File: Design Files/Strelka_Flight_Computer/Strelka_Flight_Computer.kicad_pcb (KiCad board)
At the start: 2 copper layers, 99 parts, among them J1 2-3S_LiPo_LARGE_HOLE_XT-30, J2 Conn_01x04, J5 USB_B_Micro, J6 USB_B_Micro, Q1 ??, Q10 AP2300, Q11 AP2300, Q12 AO3401A, Q2 ??, Q3 AO3401A, Q4 AP2300, Q5 AO3401A, Q6 AP2300, Q7 AO3401A, Q8 AP2300, Q9 MMBT2222, SW1 SW_Push, SW2 SW_Push, U1 FP6276BXR-G1, U10 BMX055, U13 LM334M, U14 LM334M, U15 LM334M, U16 LM321, U17 LM321, U18 LM321, U2 AP9101CK6, U3 AMS1117-3.3, U4 RFM95W-915S2, U5 STM32F405RGTx, U6 LM358, U7 USBLC6-2SC6, U8 USBLC6-2SC6, U9 CP2102N-Axx-xQFN28, Y1 Q13FC1350000200, Y2 X322524MOB4SI

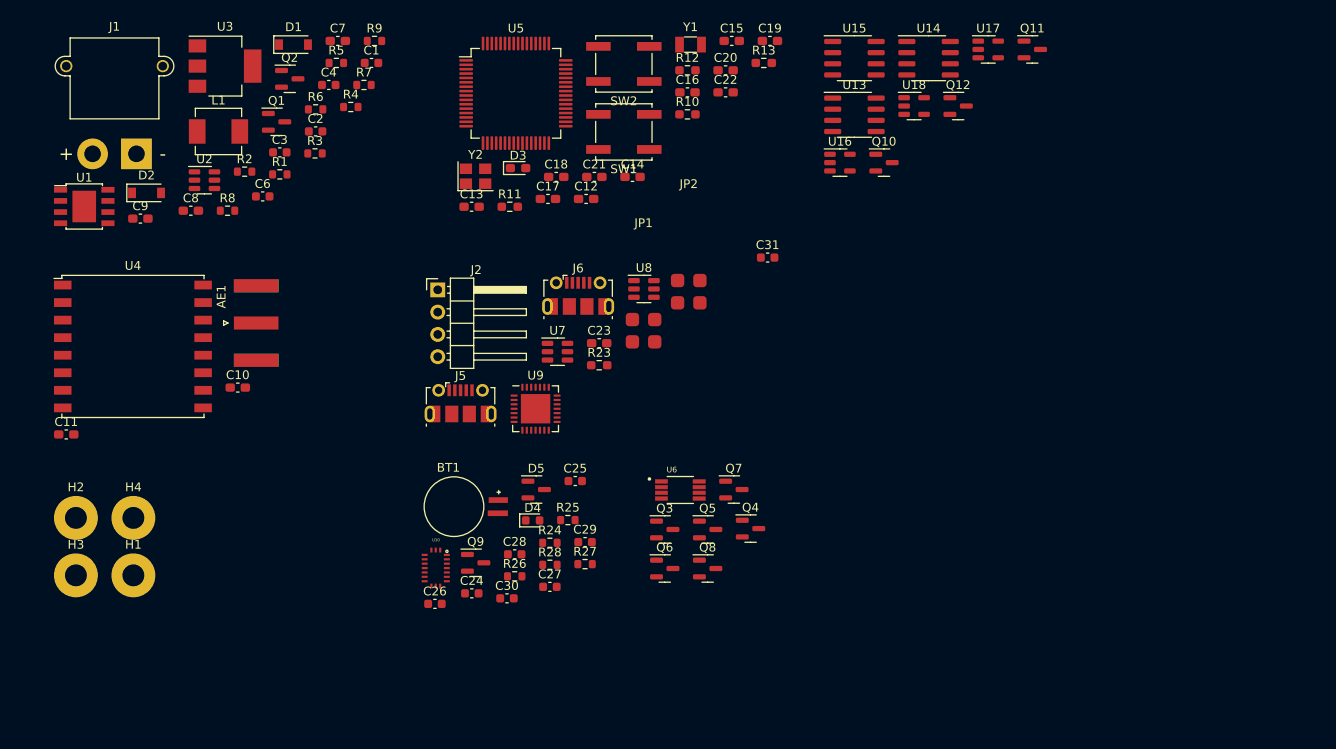
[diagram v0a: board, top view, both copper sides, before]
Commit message: Started writing libraries for board functions
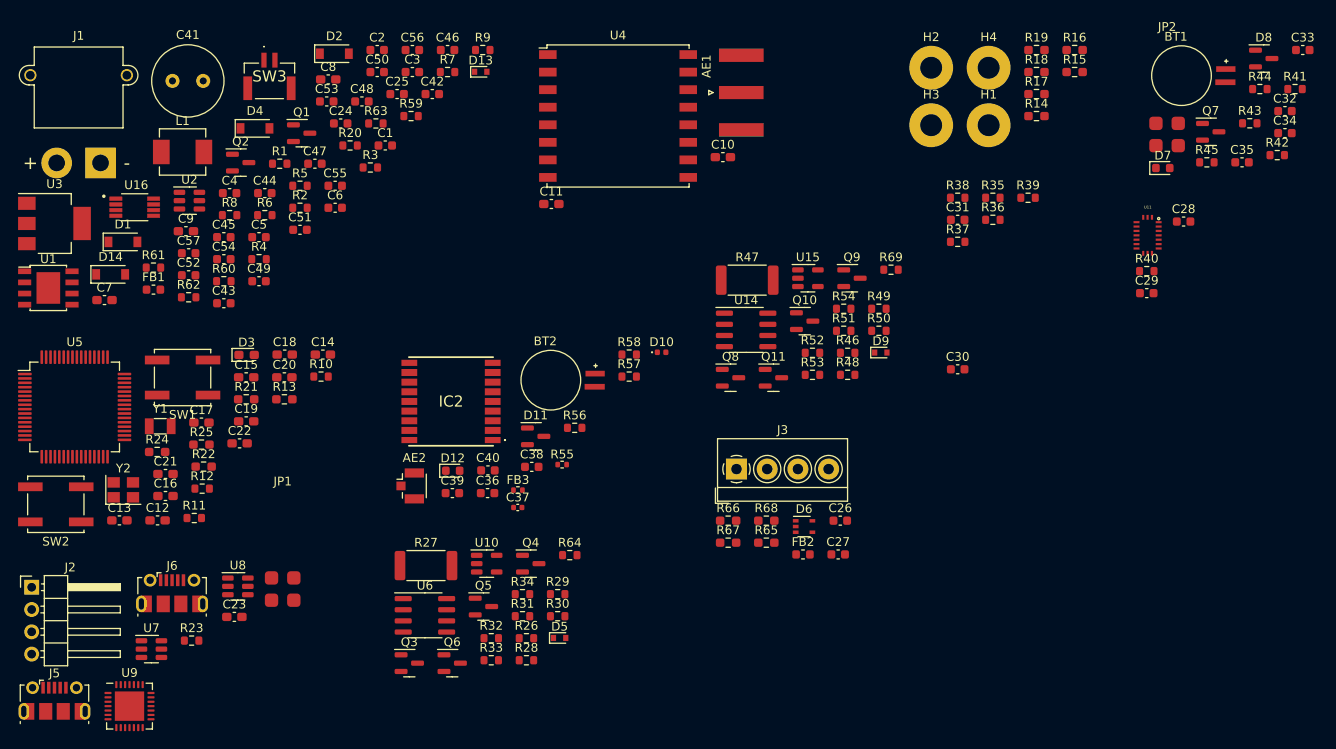
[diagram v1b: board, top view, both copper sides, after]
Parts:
- removed Q12: AO3401A, Package_TO_SOT_SMD:SOT-23
- removed U13: LM334M, Package_SO:SOIC-8_3.9x4.9mm_P1.27mm
- removed U17, U18: LM321, Package_TO_SOT_SMD:SOT-23-5
- added AE2: Antenna_Shield, Connector_Coaxial:U.FL_Hirose_U.FL-R-SMT-1_Vertical, F.Cu at (126.3, 98.8)
- added BT2: MS621FE-FL11E, Footprints:BAT_MS621FE-FL11E, F.Cu at (142.3, 86.8)
- added C32: 100nF, Capacitor_SMD:C_0603_1608Metric, F.Cu at (226.0, 56.1)
- added C33: 10uF, Capacitor_SMD:C_0603_1608Metric, F.Cu at (228.0, 49.1)
- added C34: 100n, Capacitor_SMD:C_0603_1608Metric, F.Cu at (226.0, 58.6)
- added C35: 4.7u, Capacitor_SMD:C_0603_1608Metric, F.Cu at (221.1, 62.0)
- added C36: 100n, Capacitor_SMD:C_0603_1608Metric, F.Cu at (135.1, 99.7)
- added C37: NC, Capacitor_SMD:C_0402_1005Metric, F.Cu at (138.5, 101.3)
- added C38: 4.7u, Capacitor_SMD:C_0603_1608Metric, F.Cu at (140.1, 96.7)
- added C39: 100nF, Capacitor_SMD:C_0603_1608Metric, F.Cu at (131.1, 99.7)
- added C40: 10uF, Capacitor_SMD:C_0603_1608Metric, F.Cu at (135.1, 97.1)
- added C41: 1500u, Capacitor_THT:C_Radial_D8.0mm_H11.5mm_P3.50mm, F.Cu at (99.2, 52.7)
- added C42: NC, Capacitor_SMD:C_0603_1608Metric, F.Cu at (128.8, 54.2)
- added C43: NC, Capacitor_SMD:C_0603_1608Metric, F.Cu at (105.0, 78.0)
- added C44: 2.2u, Capacitor_SMD:C_0603_1608Metric, F.Cu at (109.7, 65.5)
- added C45: 2.2u, Capacitor_SMD:C_0603_1608Metric, F.Cu at (105.0, 70.5)
- added C46: 22u, Capacitor_SMD:C_0603_1608Metric, F.Cu at (130.5, 49.1)
- added C47: 1u, Capacitor_SMD:C_0603_1608Metric, F.Cu at (115.4, 62.1)
- added C48: 0.1u, Capacitor_SMD:C_0603_1608Metric, F.Cu at (120.8, 55.0)
- added C49: NC, Capacitor_SMD:C_0603_1608Metric, F.Cu at (109.0, 75.5)
- added C5: 22u, Capacitor_SMD:C_0603_1608Metric, F.Cu at (109.0, 70.5)
- added C50: NC, Capacitor_SMD:C_0603_1608Metric, F.Cu at (122.5, 51.7)
- added C51: 820p, Capacitor_SMD:C_0603_1608Metric, F.Cu at (113.7, 69.6)
- added C52: NC, Capacitor_SMD:C_0603_1608Metric, F.Cu at (101.0, 74.8)
- added C53: NC, Capacitor_SMD:C_0603_1608Metric, F.Cu at (116.8, 55.0)
- added C54: NC, Capacitor_SMD:C_0603_1608Metric, F.Cu at (105.0, 73.0)
- added C55: 68u, Capacitor_SMD:C_0603_1608Metric, F.Cu at (117.7, 64.6)
- added C56: NC, Capacitor_SMD:C_0603_1608Metric, F.Cu at (126.5, 49.1)
- added C57: NC, Capacitor_SMD:C_0603_1608Metric, F.Cu at (101.0, 72.3)
- added D10: ESD9B3.3ST5G, Diode_SMD:D_0402_1005Metric, F.Cu at (154.9, 83.6)
- added D11: BAT54C, Package_TO_SOT_SMD:SOT-23, F.Cu at (140.6, 93.2)
- added D12: LED_BLUE, LED_SMD:LED_0603_1608Metric, F.Cu at (131.1, 97.1)
- added D13: BZT52C3V6T, Diode_SMD:D_SOD-523, F.Cu at (134.3, 51.6)
- added D14: DSK34, Diode_SMD:D_SOD-123, F.Cu at (92.1, 74.7)
- added D6: SP0504BAJT, Package_TO_SOT_SMD:SOT-353_SC-70-5, F.Cu at (171.2, 103.5)
- added D7: LED_BLUE, LED_SMD:LED_0603_1608Metric, F.Cu at (212.0, 62.6)
- added D8: BAT54C, Package_TO_SOT_SMD:SOT-23, F.Cu at (223.5, 50.1)
- added D9: 1SS388, Diode_SMD:D_SOD-523, F.Cu at (179.9, 83.6)
- added FB1: FerriteBead_Small, Inductor_SMD:L_0603_1608Metric, F.Cu at (97.0, 76.5)
- added FB2: FerriteBead_Small, Inductor_SMD:L_0603_1608Metric, F.Cu at (171.0, 106.6)
- added FB3: HZ1005K182TFB03, Resistor_SMD:R_0402_1005Metric, F.Cu at (138.5, 99.3)
- added IC2: MAX-M10S-00B, Footprints:MAXM10S00B, F.Cu at (130.9, 89.2)
- added J3: DB125-3.5-4P-GN-S, TerminalBlock_4Ucon:TerminalBlock_4Ucon_1x04_P3.50mm_Horizontal, F.Cu at (163.5, 96.9)
- added R14: 0, Resistor_SMD:R_0603_1608Metric_Pad0.98x0.95mm_HandSolder, F.Cu at (197.6, 56.7)
- added R15: 0, Resistor_SMD:R_0603_1608Metric_Pad0.98x0.95mm_HandSolder, F.Cu at (202.0, 51.7)
- added R16: 0, Resistor_SMD:R_0603_1608Metric_Pad0.98x0.95mm_HandSolder, F.Cu at (202.0, 49.1)
- added R17: 0, Resistor_SMD:R_0603_1608Metric_Pad0.98x0.95mm_HandSolder, F.Cu at (197.6, 54.2)
- added R18: 0, Resistor_SMD:R_0603_1608Metric_Pad0.98x0.95mm_HandSolder, F.Cu at (197.6, 51.7)
- added R19: 0, Resistor_SMD:R_0603_1608Metric_Pad0.98x0.95mm_HandSolder, F.Cu at (197.6, 49.1)
- added R20: 0, Resistor_SMD:R_0603_1608Metric, F.Cu at (119.4, 60.0)
- added R21: 10k, Resistor_SMD:R_0603_1608Metric_Pad0.98x0.95mm_HandSolder, F.Cu at (107.6, 89.0)
- added R22: 10k, Resistor_SMD:R_0603_1608Metric_Pad0.98x0.95mm_HandSolder, F.Cu at (102.7, 96.6)
- added R29: 100k, Resistor_SMD:R_0603_1608Metric, F.Cu at (143.1, 111.2)
- added R30: 100k, Resistor_SMD:R_0603_1608Metric, F.Cu at (143.1, 113.7)
- added R31: 1k, Resistor_SMD:R_0603_1608Metric, F.Cu at (139.1, 113.7)
- added R32: 100k, Resistor_SMD:R_0603_1608Metric, F.Cu at (135.5, 116.2)
- added R33: 1k, Resistor_SMD:R_0603_1608Metric, F.Cu at (135.5, 118.7)
- added R34: 1k, Resistor_SMD:R_0603_1608Metric, F.Cu at (139.1, 111.2)
- added R35: 47k, Resistor_SMD:R_0603_1608Metric, F.Cu at (192.7, 66.0)
- added R36: 47k, Resistor_SMD:R_0603_1608Metric, F.Cu at (192.7, 68.5)
- added R37: 47k, Resistor_SMD:R_0603_1608Metric, F.Cu at (188.7, 71.0)
- added R38: 47k, Resistor_SMD:R_0603_1608Metric, F.Cu at (188.7, 66.0)
- added R39: 47k, Resistor_SMD:R_0603_1608Metric, F.Cu at (196.7, 66.0)
- added R40: 0R, Resistor_SMD:R_0603_1608Metric, F.Cu at (210.2, 74.3)
- added R41: 1k, Resistor_SMD:R_0603_1608Metric, F.Cu at (227.1, 53.6)
- added R42: R_Small, Resistor_SMD:R_0603_1608Metric, F.Cu at (225.1, 61.1)
- added R43: 1k, Resistor_SMD:R_0603_1608Metric, F.Cu at (222.0, 57.5)
- added R44: 1k, Resistor_SMD:R_0603_1608Metric, F.Cu at (223.1, 53.6)
- added R45: 1k, Resistor_SMD:R_0603_1608Metric, F.Cu at (217.1, 62.0)
- added R46: 64.9R, Resistor_SMD:R_0603_1608Metric, F.Cu at (176.1, 83.7)
- added R47: 2R, Resistor_SMD:R_2512_6332Metric, F.Cu at (164.7, 75.4)
- added R48: 1k, Resistor_SMD:R_0603_1608Metric, F.Cu at (176.1, 86.2)
- added R49: 100k, Resistor_SMD:R_0603_1608Metric, F.Cu at (179.7, 78.6)
- added R50: 100k, Resistor_SMD:R_0603_1608Metric, F.Cu at (179.7, 81.2)
- added R51: 1k, Resistor_SMD:R_0603_1608Metric, F.Cu at (175.7, 81.2)
- added R52: 100k, Resistor_SMD:R_0603_1608Metric, F.Cu at (172.1, 83.7)
- added R53: 1k, Resistor_SMD:R_0603_1608Metric, F.Cu at (172.1, 86.2)
- added R54: 1k, Resistor_SMD:R_0603_1608Metric, F.Cu at (175.7, 78.6)
- added R55: 0R, Resistor_SMD:R_0402_1005Metric, F.Cu at (143.6, 96.4)
- added R56: 1k, Resistor_SMD:R_0603_1608Metric, F.Cu at (145.0, 92.2)
- added R57: 1k, Resistor_SMD:R_0603_1608Metric, F.Cu at (151.2, 86.4)
- added R58: 0R, Resistor_SMD:R_0603_1608Metric, F.Cu at (151.2, 83.9)
- added R59: 13k, Resistor_SMD:R_0603_1608Metric, F.Cu at (126.4, 56.7)
- added R60: 47k, Resistor_SMD:R_0603_1608Metric, F.Cu at (105.0, 75.5)
- added R61: 56.2k, Resistor_SMD:R_0603_1608Metric, F.Cu at (97.0, 74.0)
- added R62: 82k, Resistor_SMD:R_0603_1608Metric, F.Cu at (101.0, 77.3)
- added R63: 27k, Resistor_SMD:R_0603_1608Metric, F.Cu at (122.4, 57.5)
- added R64: 100k, Resistor_SMD:R_0603_1608Metric, F.Cu at (144.5, 106.7)
- added R65: 33, Resistor_SMD:R_0603_1608Metric_Pad0.98x0.95mm_HandSolder, F.Cu at (166.9, 105.3)
- added R66: 33, Resistor_SMD:R_0603_1608Metric_Pad0.98x0.95mm_HandSolder, F.Cu at (162.5, 102.8)
- added R67: 33, Resistor_SMD:R_0603_1608Metric_Pad0.98x0.95mm_HandSolder, F.Cu at (162.5, 105.3)
- added R68: 33, Resistor_SMD:R_0603_1608Metric_Pad0.98x0.95mm_HandSolder, F.Cu at (166.9, 102.8)
- added R69: 100k, Resistor_SMD:R_0603_1608Metric, F.Cu at (181.1, 74.2)
- added SW3: SW_DIP_x01, Footprints:SM02BGHSTBLFSN, F.Cu at (110.2, 52.1)
- added U11: BMX055, Footprints:BMX055, F.Cu at (210.3, 70.3)
- C24, C25: value 100nF -> NC
- C26, C27: value 100nF -> 2.2u
- C28: value 10uF -> 100nF
- C29: value 100n -> 100nF
- C30: value 4.7u -> 100nF
- C4: value 22u -> NC
- D4: value LED_BLUE -> B5819W; footprint LED_SMD:LED_0603_1608Metric -> Diode_SMD:D_SOD-123
- D5: value BAT54C -> 1SS388; footprint Package_TO_SOT_SMD:SOT-23 -> Diode_SMD:D_SOD-523
- J1: value 2-3S_LiPo_LARGE_HOLE_XT-30 -> 1S_LiPo_LARGE_HOLE_XT-30
- Q11, Q6: value AP2300 -> MMBT2222
- Q4, Q8: value AP2300 -> AO3401A
- Q5: value AO3401A -> AP2300
- Q7: value AO3401A -> MMBT2222
- Q9: value MMBT2222 -> AO3401A
- R10, R11, R12, R23: footprint Resistor_SMD:R_0603_1608Metric_Pad0.98x0.95mm_HandSolder -> Resistor_SMD:R_0603_1608Metric
- R24: value 1k -> NC; footprint Resistor_SMD:R_0603_1608Metric -> Resistor_SMD:R_0603_1608Metric_Pad0.98x0.95mm_HandSolder
- R25: value R_Small -> 10k; footprint Resistor_SMD:R_0603_1608Metric -> Resistor_SMD:R_0603_1608Metric_Pad0.98x0.95mm_HandSolder
- R26: value 1k -> 64.9R
- R27: value 1k -> 2R; footprint Resistor_SMD:R_0603_1608Metric -> Resistor_SMD:R_2512_6332Metric
- U10: value BMX055 -> LM321; footprint Footprints:BMX055 -> Package_TO_SOT_SMD:SOT-23-5
- U15: value LM334M -> LM321; footprint Package_SO:SOIC-8_3.9x4.9mm_P1.27mm -> Package_TO_SOT_SMD:SOT-23-5
- U16: value LM321 -> TPS61085DGKR; footprint Package_TO_SOT_SMD:SOT-23-5 -> Footprints:SOP65P490X110-8N
- U6: value LM358 -> LM334M; footprint Footprints:SOP65P490X110-8N -> Package_SO:SOIC-8_3.9x4.9mm_P1.27mm
- moved H1 110.2 mm to (192.2, 57.7)
- moved H2 110.2 mm to (185.6, 51.2)
- moved H3 110.2 mm to (185.6, 57.7)
- moved H4 110.2 mm to (192.2, 51.2)
- moved BT1 96.4 mm to (214.2, 52.1)
- moved C28 85.1 mm to (214.4, 68.7)
- moved SW2 81.9 mm to (85.9, 100.9)
- moved U16 80.5 mm to (94.9, 67.1)
- moved C16 75.2 mm to (98.4, 100.0)
- moved Y1 74.5 mm to (97.8, 92.0)
- moved C19 73.8 mm to (107.6, 91.5)
- moved R12 73.0 mm to (102.6, 99.1)
- moved C29 70.0 mm to (210.2, 76.9)
- moved C22 68.3 mm to (106.8, 94.0)
- moved Q7 67.9 mm to (217.5, 58.5)
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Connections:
- net /Continuity_Testing/AUX+ renamed Net-(D9-Pad2)
- net /Data_Interfaces/RX_RADIO renamed /Data_Interfaces/TX_CP2102
- net /Data_Interfaces/TX_RADIO renamed /Data_Interfaces/RX_CP2102
- net /Power/BUCK_EN renamed /Power/BOOST_EN
- net Net-(Q7-Pad2) renamed /Sensors/L80-M39/GPS_RESET
- BT1 pad +: /Sensors/V_BKCP -> /Sensors/L80-M39/V_BKCP
- C24 pad 1: VDD -> VDC
- C25 pad 1: VDD -> VDC
- C26 pad 1: VDD -> GND
- C26 pad 2: GND -> +5VD
- C27 pad 1: VDD -> GND
- C27 pad 2: GND -> Net-(C27-Pad2)
- C28 pad 1: VDD -> +3V3
- C29 pad 1: /Sensors/V_BKCP -> +3V3
- C30 pad 1: /Sensors/V_BKCP -> +3V3
- C31 pad 1: VDD -> +3V3
- C4 pad 1: GND -> VDC
- C4 pad 2: +5VA -> GND
- D1 pad 1: VDC -> Net-(D1-Pad1)
- D4 pad 1: GND -> VBUS
- D4 pad 2: Net-(D4-Pad2) -> +5VD
- D5 pad 1: VDD -> /Actuators/Ematch_Drogue1/EMATCH+
- D5 pad 2: unconnected-(D5-Pad2) -> Net-(D5-Pad2)
- JP2 pad 1: Net-(JP2-Pad1) -> /Sensors/RXD2_GPS
- JP2 pad 2: /Data_Interfaces/RTS_RADIO -> Net-(JP2-Pad2)
- JP2 pad 3: Net-(JP2-Pad3) -> /Sensors/TXD2_GPS
- JP2 pad 4: /Data_Interfaces/CTS_RADIO -> Net-(JP2-Pad4)
- Q1 pad 2: VDC -> Net-(D1-Pad1)
- Q10 pad 3: /Continuity_Testing/DROGUE- -> /Actuators/Ematch_Main/EMATCH-
- Q11 pad 2: GND -> Net-(Q11-Pad2)
- Q11 pad 3: /Continuity_Testing/AUX- -> GND
- Q2 pad 3: +5VA -> Net-(Q2-Pad3)
- Q3 pad 2: Net-(Q3-Pad2) -> +3V3
- Q3 pad 3: /Actuators/MAIN+ -> Net-(Q3-Pad3)
- Q4 pad 2: GND -> Net-(Q4-Pad2)
- Q4 pad 3: /Actuators/MAIN- -> /Actuators/Ematch_Drogue1/EMATCH+
- Q5 pad 2: Net-(Q5-Pad2) -> GND
- Q5 pad 3: /Actuators/DROGUE+ -> /Actuators/Ematch_Drogue1/EMATCH-
- Q6 pad 2: GND -> Net-(Q4-Pad1)
- Q6 pad 3: /Actuators/DROGUE- -> GND
- Q7 pad 3: /Actuators/AUX+ -> GND
- Q8 pad 2: GND -> +3V3
- Q8 pad 3: /Actuators/AUX- -> Net-(Q8-Pad3)
- Q9 pad 1: Net-(Q9-Pad1) -> Net-(Q11-Pad2)
- Q9 pad 2: /Sensors/GPS_RESET -> Net-(Q9-Pad2)
- Q9 pad 3: GND -> /Actuators/Ematch_Main/EMATCH+
- R10 pad 1: GND -> Net-(R10-Pad1)
- R10 pad 2: Net-(R10-Pad2) -> GND
- R23 pad 1: Net-(R23-Pad1) -> +3V3
- R23 pad 2: +3V3 -> Net-(R23-Pad2)
- R24 pad 1: Net-(R24-Pad1) -> /STM32F405/SD_DET
- R24 pad 2: Net-(D4-Pad2) -> +3V3
- R25 pad 1: Net-(R24-Pad1) -> GND
- R25 pad 2: /Sensors/GPS_PPS -> /STM32F405/SD_DET
- R26 pad 1: /Sensors/GPS_RST -> Net-(D5-Pad2)
- R26 pad 2: Net-(Q9-Pad1) -> Net-(R26-Pad2)
- R27 pad 1: Net-(Q9-Pad1) -> VDC
- R27 pad 2: GND -> Net-(Q4-Pad2)
- R28 pad 1: /Sensors/V_BKCP -> Net-(Q3-Pad1)
- R28 pad 2: Net-(D5-Pad3) -> /Actuators/CONT_TEST_EN
- R5 pad 2: +5VA -> Net-(C44-Pad2)
- SW1 pad 2: Net-(R10-Pad2) -> Net-(R10-Pad1)
- U1 pad 8: +5VA -> Net-(C44-Pad2)
- U10 pad 1: /Sensors/BMX_Int_2 -> /Actuators/Ematch_Drogue1/EMATCH+
- U10 pad 2: /Sensors/BMX_DRDYM -> +3V3
- U10 pad 3: VDD -> Net-(R32-Pad2)
- U10 pad 4: GND -> /Actuators/DROGUE_CONT
- U10 pad 5: unconnected-(U10-Pad5) -> GND
- U14 pad 4: VDC -> Net-(Q8-Pad3)
- U15 pad 1: unconnected-(U15-Pad1) -> /Actuators/Ematch_Main/EMATCH+
- U15 pad 2: /Continuity_Testing/MAIN+ -> +3V3
- U15 pad 3: /Continuity_Testing/MAIN+ -> Net-(R52-Pad2)
- U15 pad 4: Net-(Q12-Pad3) -> /Actuators/MAIN_CONT
- U15 pad 5: (no net) -> GND
- U16 pad 2: +3V3 -> Net-(R62-Pad1)
- U16 pad 3: Net-(R30-Pad2) -> VDC
- U16 pad 4: /Continuity_Testing/DROGUE_Cont -> GND
- U16 pad 5: GND -> Net-(D14-Pad2)
- U5 pad 1: unconnected-(U5-Pad1) -> +3V3
- U5 pad 10: unconnected-(U5-Pad10) -> /STM32F405/SPI2_MISO
- U5 pad 11: unconnected-(U5-Pad11) -> /STM32F405/SPI2_MOSI
- U5 pad 14: /Data_Interfaces/CTS_2 -> /Actuators/MAIN_L
- U5 pad 15: /Data_Interfaces/RTS_2 -> /Actuators/MAIN_H
- U5 pad 16: /Data_Interfaces/TX_2 -> /Actuators/DROGUE_CONT
- U5 pad 17: /Data_Interfaces/RX_2 -> /Actuators/MAIN_CONT
- U5 pad 2: unconnected-(U5-Pad2) -> /Actuators/CONT_TEST_EN
- U5 pad 24: unconnected-(U5-Pad24) -> /STM32F405/INT_IN1
- U5 pad 25: unconnected-(U5-Pad25) -> /STM32F405/INT_IN2
- U5 pad 26: /915MHz_Radio/RESET_RF -> unconnected-(U5-Pad26)
- U5 pad 27: /915MHz_Radio/IO0_RF -> unconnected-(U5-Pad27)
- U5 pad 29: /915MHz_Radio/IO1_RF -> /STM32F405/I2C2_SCL
- U5 pad 30: /915MHz_Radio/IO2_RF -> /STM32F405/I2C2_SDA
- U5 pad 33: /915MHz_Radio/IO3_RF -> /STM32F405/SPI2_NSS4
- U5 pad 34: /915MHz_Radio/IO4_RF -> /STM32F405/SPI2_SCK
- U5 pad 37: unconnected-(U5-Pad37) -> /STM32F405/INT_IN3
- U5 pad 38: unconnected-(U5-Pad38) -> /STM32F405/SD_DET
- U5 pad 39: unconnected-(U5-Pad39) -> /STM32F405/SDIO_D0
- U5 pad 40: unconnected-(U5-Pad40) -> /STM32F405/SDIO_D1
- U5 pad 41: /915MHz_Radio/IO5_RF -> /Actuators/DROGUE_H
- U5 pad 44: /Data_Interfaces/CTS_RADIO -> /915MHz_Radio/IO0_RF
- U5 pad 45: /Data_Interfaces/RTS_RADIO -> /STM32F405/SPI2_NSS3
- U5 pad 50: unconnected-(U5-Pad50) -> /Actuators/EXT_SPI_CS
- U5 pad 51: unconnected-(U5-Pad51) -> /STM32F405/SDIO_D2
- U5 pad 52: unconnected-(U5-Pad52) -> /STM32F405/SDIO_D3
- U5 pad 53: unconnected-(U5-Pad53) -> /STM32F405/SDIO_CK
- U5 pad 54: /STM32F405/INDICATOR_LED -> /STM32F405/SDIO_CMD
- U5 pad 55: unconnected-(U5-Pad55) -> /Actuators/EXT_SPI_SCK
- U5 pad 56: unconnected-(U5-Pad56) -> /Actuators/EXT_SPI_MISO
- U5 pad 57: unconnected-(U5-Pad57) -> /Actuators/EXT_SPI_MOSI
- U5 pad 58: unconnected-(U5-Pad58) -> /Actuators/DROGUE_L
- U5 pad 59: unconnected-(U5-Pad59) -> /STM32F405/GPIO_PB7
- U5 pad 60: Net-(R10-Pad2) -> Net-(R10-Pad1)
- U5 pad 61: unconnected-(U5-Pad61) -> /STM32F405/SPI2_NSS1
- U5 pad 62: unconnected-(U5-Pad62) -> /STM32F405/SPI2_NSS2
- U5 pad 8: unconnected-(U5-Pad8) -> /Power/BATT_VOLT
- U5 pad 9: unconnected-(U5-Pad9) -> /STM32F405/INDICATOR_LED
- U6 pad 1: unconnected-(U6-Pad1) -> Net-(R26-Pad2)
- U6 pad 2: unconnected-(U6-Pad2) -> Net-(D5-Pad2)
- U6 pad 3: unconnected-(U6-Pad3) -> Net-(D5-Pad2)
- U6 pad 4: unconnected-(U6-Pad4) -> Net-(Q3-Pad3)
- U6 pad 5: unconnected-(U6-Pad5) -> (no net)
- U6 pad 6: unconnected-(U6-Pad6) -> Net-(D5-Pad2)
- U6 pad 7: unconnected-(U6-Pad7) -> Net-(D5-Pad2)
- U6 pad 8: unconnected-(U6-Pad8) -> (no net)
- U9 pad 23: Net-(JP2-Pad3) -> unconnected-(U9-Pad23)
- U9 pad 24: Net-(JP2-Pad1) -> unconnected-(U9-Pad24)
- U9 pad 9: Net-(R23-Pad1) -> Net-(R23-Pad2)

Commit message: Started component placement
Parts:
- removed BT1: MS621FE-FL11E, Footprints:BAT_MS621FE-FL11E
- removed C24, C25, C42, C43: NC, Capacitor_SMD:C_0603_1608Metric
- removed C32: 100nF, Capacitor_SMD:C_0603_1608Metric
- removed C33: 10uF, Capacitor_SMD:C_0603_1608Metric
- removed C34: 100n, Capacitor_SMD:C_0603_1608Metric
- removed C35: 4.7u, Capacitor_SMD:C_0603_1608Metric
- removed C44, C45: 2.2u, Capacitor_SMD:C_0603_1608Metric
- removed C5: 22u, Capacitor_SMD:C_0603_1608Metric
- removed D7: LED_BLUE, LED_SMD:LED_0603_1608Metric
- removed D8: BAT54C, Package_TO_SOT_SMD:SOT-23
- removed L1: 3.3u, Inductor_SMD:L_Vishay_IHLP-2020
- removed Q7: MMBT2222, Package_TO_SOT_SMD:SOT-23
- removed R1, R6: 10k, Resistor_SMD:R_0603_1608Metric
- removed R2: NC, Resistor_SMD:R_0603_1608Metric
- removed R26, R46: 64.9R, Resistor_SMD:R_0603_1608Metric
- removed R4: 37.5k, Resistor_SMD:R_0603_1608Metric
- removed R41, R43, R44, R45: 1k, Resistor_SMD:R_0603_1608Metric
- removed R42: R_Small, Resistor_SMD:R_0603_1608Metric
- removed R5: 73.2k, Resistor_SMD:R_0603_1608Metric
- removed U1: FP6276BXR-G1, Package_SO:Diodes_PSOP-8
- removed U14, U6: LM334M, Package_SO:SOIC-8_3.9x4.9mm_P1.27mm
- added I1: AL5809-30S1-7, Diode_SMD:D_SOD-123, F.Cu at (-71.1, 55.9)
- added I2: AL5809-30S1-7, Diode_SMD:D_SOD-123, F.Cu at (-61.1, 55.9)
- added IC1: XTSD04GLGEAG, Footprints:SON127P800X600X95-8N, F.Cu at (48.3, 55.9)
- added J4: SM06B-GHS-TB(LF)(SN), Footprints:JST_SM06B-GHS-TB(LF)(SN), F.Cu at (195.6, 68.6)
- added JP2: UART_Switch, Footprints:UART_Switch, F.Cu at (-99.1, 50.8)
- added L2: 6u, Inductor_SMD:L_Bourns_SRP5030T, F.Cu at (149.9, 73.7)
- added MOSFET1: DMG6968UDM-7, Footprints:DMG6968UDM-7, F.Cu at (116.8, 73.7)
- added U12: MS561101BA03-50, Footprints:MS561101BA03-50, F.Cu at (243.8, 68.6)
- AE1: footprint Connector_Coaxial:SMA_Amphenol_132289_EdgeMount -> Connector_Coaxial:SMA_Amphenol_132134_Vertical
- C1: value 22u -> 2.2u
- C2: value 1n -> 1u
- C3: value NC -> 10n
- C4: value NC -> 2.2u
- FB1, FB2: value FerriteBead_Small -> BLM18PG221SN1D
- moved C1 272.1 mm to (-147.3, 33.0)
- moved C3 270.5 mm to (-143.3, 33.0)
- moved C2 266.2 mm to (-143.3, 35.5)
- moved C4 254.5 mm to (-147.3, 38.0)
- moved FB1 247.7 mm to (-147.3, 35.5)
- moved C13 226.7 mm to (-132.3, 79.2)
- moved C54 226.7 mm to (-120.4, 49.5)
- moved D13 226.7 mm to (-91.2, 28.1)
- moved J2 226.7 mm to (-142.3, 86.9)
- moved JP2 226.7 mm to (-12.9, 35.3)
- moved Q3 226.7 mm to (-99.3, 95.5)
- moved Q5 226.7 mm to (-90.8, 89.1)
- moved Q6 226.7 mm to (-94.4, 95.5)
- moved Q8 226.7 mm to (-62.7, 63.0)
- moved Q9 226.7 mm to (-48.8, 51.6)
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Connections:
- net /Sensors/RXD2_GPS renamed Net-(IC2-Pad3)
- net /Sensors/TXD2_GPS renamed Net-(IC2-Pad2)
- AE2 pad 1: /Sensors/MAX-M10S-00B/VCC_RF -> /Sensors/MAX-M10S-00B/RF_IN
- C1 pad 1: VDC -> GND
- C1 pad 2: GND -> Net-(U5-Pad13)
- C2 pad 1: Net-(C2-Pad1) -> Net-(U5-Pad13)
- C3 pad 1: Net-(C3-Pad1) -> Net-(U5-Pad13)
- C4 pad 1: VDC -> GND
- C4 pad 2: GND -> +3V3
- D10 pad 2: /Sensors/MAX-M10S-00B/VCC_RF -> /Sensors/MAX-M10S-00B/RF_IN
- FB1 pad 1: Net-(C44-Pad2) -> +3V3
- FB1 pad 2: +5VA -> Net-(U5-Pad13)
- FB3 pad 1: /Sensors/MAX-M10S-00B/VCC_RF -> /Sensors/MAX-M10S-00B/RF_IN
- J3 pad 1: /Actuators/Ematch_Main/EMATCH- -> unconnected-(J3-Pad1)
- J3 pad 3: /Actuators/Ematch_Drogue1/EMATCH- -> unconnected-(J3-Pad3)
- J3 pad 4: /Actuators/Ematch_Drogue1/EMATCH+ -> unconnected-(J3-Pad4)
- JP2 pad 2: Net-(JP2-Pad2) -> /STM32F405/USART2_RX
- JP2 pad 4: Net-(JP2-Pad4) -> /STM32F405/USART2_TX
- R28 pad 2: /Actuators/CONT_TEST_EN -> /Actuators/Ematch_Drogue1/CONT_TEST
- R30 pad 2: /Actuators/DROGUE_L -> /Actuators/Ematch_Drogue1/FIRE_L
- R31 pad 2: /Actuators/DROGUE_L -> /Actuators/Ematch_Drogue1/FIRE_L
- R32 pad 1: /Actuators/DROGUE_CONT -> /Actuators/Ematch_Drogue1/EMATCH_Cont
- R33 pad 2: /Actuators/DROGUE_H -> /Actuators/Ematch_Drogue1/FIRE_H
- R48 pad 2: /Actuators/CONT_TEST_EN -> /Actuators/Ematch_Main/CONT_TEST
- R50 pad 2: /Actuators/MAIN_L -> /Actuators/Ematch_Main/FIRE_L
- R51 pad 2: /Actuators/MAIN_L -> /Actuators/Ematch_Main/FIRE_L
- R52 pad 1: /Actuators/MAIN_CONT -> /Actuators/Ematch_Main/EMATCH_Cont
- R53 pad 2: /Actuators/MAIN_H -> /Actuators/Ematch_Main/FIRE_H
- R58 pad 2: /STM32F405/INT_IN5 -> /STM32F405/GPIO_PB7
- R64 pad 1: /Actuators/CONT_TEST_EN -> /Actuators/Ematch_Drogue1/CONT_TEST
- R69 pad 1: /Actuators/CONT_TEST_EN -> /Actuators/Ematch_Main/CONT_TEST
- U10 pad 4: /Actuators/DROGUE_CONT -> /Actuators/Ematch_Drogue1/EMATCH_Cont
- U15 pad 4: /Actuators/MAIN_CONT -> /Actuators/Ematch_Main/EMATCH_Cont
- U5 pad 13: +3V3 -> Net-(U5-Pad13)
- U5 pad 16: /Actuators/DROGUE_CONT -> /STM32F405/USART2_TX
- U5 pad 17: /Actuators/MAIN_CONT -> /STM32F405/USART2_RX
- U5 pad 26: unconnected-(U5-Pad26) -> /Actuators/DROGUE_CONT
- U5 pad 27: unconnected-(U5-Pad27) -> /Actuators/MAIN_CONT

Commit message: First go at routing
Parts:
- C41: footprint Capacitor_THT:C_Radial_D8.0mm_H11.5mm_P3.50mm -> Footprints:ULR158M0JF1ARR
- C6, D5, D9, I1, I2, MOSFET1, Q10, Q11, Q3, Q4, Q5, Q6, Q8, Q9, R27, R28, R29, R30, R31, R32, R33, R34, R47, R48, R49, R50, R51, R52, R53, R54, R64, R69, R7, R9, U10, U15, U2, U4: moved to B.Cu
- moved C1 291.8 mm to (126.2, 134.6)
- moved C10 291.8 mm to (209.9, 139.5)
- moved C11 291.8 mm to (190.4, 144.8)
- moved C12 291.8 mm to (145.5, 180.9)
- moved C13 291.8 mm to (141.2, 180.9)
- moved C14 291.8 mm to (164.3, 162.0)
- moved C15 291.8 mm to (155.6, 164.6)
- moved C16 291.8 mm to (146.4, 178.1)
- moved C17 291.8 mm to (150.5, 169.7)
- moved C18 291.8 mm to (160.0, 162.0)
- moved C2 291.8 mm to (130.2, 137.2)
- moved C3 291.8 mm to (130.2, 134.6)
- moved C30 291.8 mm to (236.7, 163.6)
- moved C31 291.8 mm to (236.7, 146.6)
- moved C4 291.8 mm to (126.2, 139.7)
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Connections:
- J3 pad 1: unconnected-(J3-Pad1) -> /Actuators/Ematch_Main/EMATCH-
- J3 pad 3: unconnected-(J3-Pad3) -> /Actuators/Ematch_Drogue1/EMATCH-
- J3 pad 4: unconnected-(J3-Pad4) -> /Actuators/Ematch_Drogue1/EMATCH+
- R28 pad 2: /Actuators/Ematch_Drogue1/CONT_TEST -> /Actuators/CONT_TEST_EN
- R30 pad 2: /Actuators/Ematch_Drogue1/FIRE_L -> /Actuators/DROGUE_L
- R31 pad 2: /Actuators/Ematch_Drogue1/FIRE_L -> /Actuators/DROGUE_L
- R32 pad 1: /Actuators/Ematch_Drogue1/EMATCH_Cont -> /Actuators/DROGUE_CONT
- R33 pad 2: /Actuators/Ematch_Drogue1/FIRE_H -> /Actuators/DROGUE_H
- R48 pad 2: /Actuators/Ematch_Main/CONT_TEST -> /Actuators/CONT_TEST_EN
- R50 pad 2: /Actuators/Ematch_Main/FIRE_L -> /Actuators/MAIN_L
- R51 pad 2: /Actuators/Ematch_Main/FIRE_L -> /Actuators/MAIN_L
- R52 pad 1: /Actuators/Ematch_Main/EMATCH_Cont -> /Actuators/MAIN_CONT
- R53 pad 2: /Actuators/Ematch_Main/FIRE_H -> /Actuators/MAIN_H
- R64 pad 1: /Actuators/Ematch_Drogue1/CONT_TEST -> /Actuators/CONT_TEST_EN
- R69 pad 1: /Actuators/Ematch_Main/CONT_TEST -> /Actuators/CONT_TEST_EN
- U10 pad 4: /Actuators/Ematch_Drogue1/EMATCH_Cont -> /Actuators/DROGUE_CONT
- U15 pad 4: /Actuators/Ematch_Main/EMATCH_Cont -> /Actuators/MAIN_CONT
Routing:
- net VDC: track 0.00 -> 63.9 mm, vias 0 -> 1
- net /Actuators/DROGUE_H: track 0.00 -> 45.1 mm, vias 0 -> 2
- net /Actuators/DROGUE_CONT: track 0.00 -> 36.8 mm, vias 0 -> 1
- net /Actuators/CONT_TEST_EN: track 0.00 -> 36.3 mm, vias 0 -> 2
- net /Actuators/Ematch_Main/EMATCH+: track 0.00 -> 30.3 mm
- net VBUS: track 0.00 -> 24.4 mm
- net /Actuators/MAIN_CONT: track 0.00 -> 23.7 mm, vias 0 -> 1
- net /Actuators/DROGUE_L: track 0.00 -> 21.2 mm, vias 0 -> 2
- net /Actuators/MAIN_L: track 0.00 -> 19.9 mm, vias 0 -> 2
- net /STM32F405/USB2_IN+: track 0.00 -> 19.5 mm
- net /Actuators/Ematch_Drogue1/EMATCH+: track 0.00 -> 19.4 mm
- net /STM32F405/USB2_IN-: track 0.00 -> 18.3 mm
- net +BATT: track 0.00 -> 17.9 mm
- net Net-(Q11-Pad2): track 0.00 -> 13.7 mm
- net Net-(I2-Pad1): track 0.00 -> 13.6 mm
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- added copper zone on F.Cu, net +3V3
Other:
- board outline added: 124.4 x 38.4 mm
- copper layers 2 -> 4
- board text added: "+"
- board text added: "-"
- board text added: "4.2Vin MAX"
- board text added: "Batt PWR Select"
- board text added: "PWR SW"
